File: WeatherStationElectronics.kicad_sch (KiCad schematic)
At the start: 4 parts, among them U1 ESP32-C3-DevKitM-1, U3 DHT11, U4 BMP280

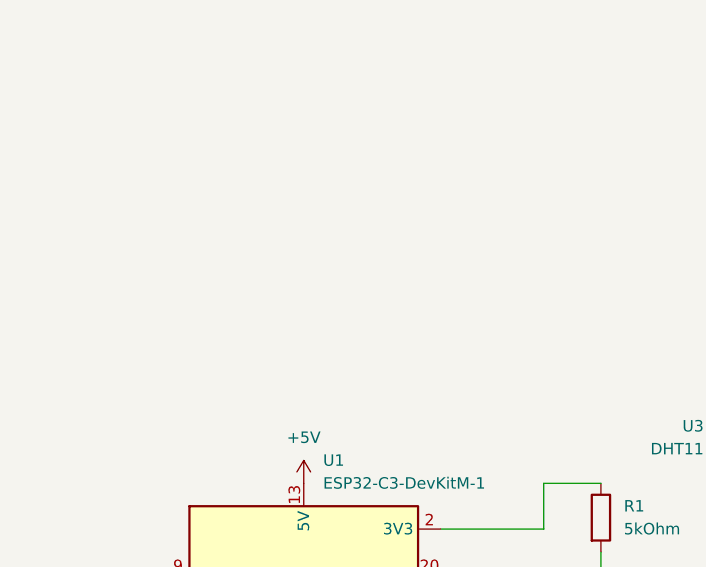
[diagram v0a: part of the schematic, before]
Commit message: first PCB
todo: add a power switch
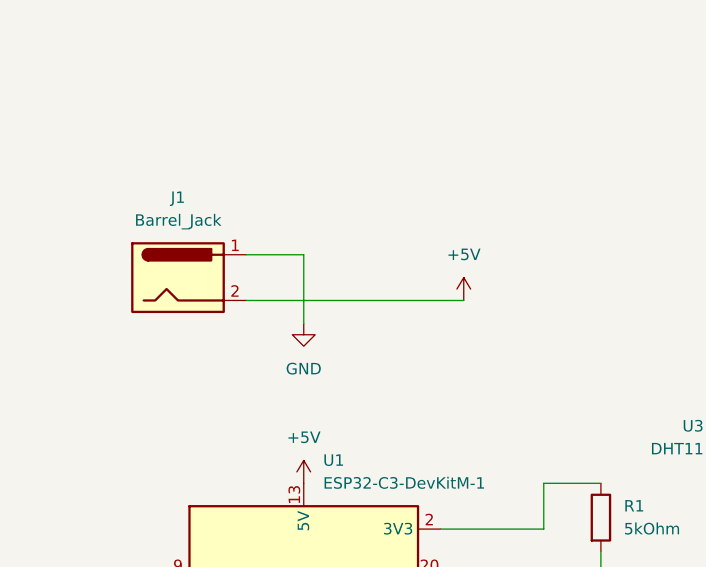
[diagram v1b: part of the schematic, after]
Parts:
- added J1: Barrel_Jack, Connector_BarrelJack:BarrelJack_CUI_PJ-063AH_Horizontal, symbol Connector:Barrel_Jack
- R1: footprint (none) -> Resistor_THT:R_Axial_DIN0411_L9.9mm_D3.6mm_P7.62mm_Vertical
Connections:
- net +5V: now also J1.2
- net GND: now also J1.1
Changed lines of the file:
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@@
+	(wire
+		(pts
+			(xy 68.58 41.91) (xy 68.58 34.29)
+		)
+		(stroke
+			(width 0)
+			(type default)
+		)
+	)
 	(wire
 		(pts
@@
 	(wire
 		(pts
+			(xy 62.23 39.37) (xy 86.36 39.37)
+		)
+		(stroke
+			(width 0)
+			(type default)
+		)
+	)
+	(wire
+		(pts
 			(xy 127 54.61) (xy 127 69.85)
+		)
+		(stroke
+			(width 0)
+			(type default)
+		)
+	)
+	(wire
+		(pts
+			(xy 68.58 34.29) (xy 62.23 34.29)
 		)
 		(stroke
@@
 	)
 	(symbol
+		(lib_id "power:GND")
+		(at 68.58 41.91 0)
+		(unit 1)
+		(exclude_from_sim no)
+		(in_bom yes)
+		(on_board yes)
+		(dnp no)
+		(fields_autoplaced yes)
+		(property "Reference" "#PWR03"
+			(at 68.58 48.26 0)
+			(effects
+				(font
+					(size 1.27 1.27)
+				)
+				(hide yes)
+			)
+		)
+		(property "Value" "GND"
+			(at 68.58 46.99 0)
+			(effects
+				(font
+					(size 1.27 1.27)
+				)
+			)
+		)
+		(property "Footprint" ""
+			(at 68.58 41.91 0)
+			(effects
+				(font
+					(size 1.27 1.27)
+				)
+				(hide yes)
+			)
+		)
+		(property "Datasheet" ""
+			(at 68.58 41.91 0)
+			(effects
+				(font
+					(size 1.27 1.27)
+				)
+				(hide yes)
+			)
+		)
+		(property "Description" "Power symbol creates a global label with name \"GND\" , ground"
+			(at 68.58 41.91 0)
+			(effects
+				(font
+					(size 1.27 1.27)
+				)
+				(hide yes)
+			)
+		)
+		(pin "1"
+		)
+		(instances
+			(project ""
+				(path "/efe9557b-147a-46e1-836e-45cae14ec1c3"
+					(reference "#PWR03")
+					(unit 1)
+				)
+			)
+		)
+	)
+	(symbol
 		(lib_id "power:+5V")
 		(at 68.58 59.69 0)
@@
 	)
 	(symbol
+		(lib_id "Connector:Barrel_Jack")
+		(at 54.61 36.83 0)
+		(unit 1)
+		(exclude_from_sim no)
+		(in_bom yes)
+		(on_board yes)
+		(dnp no)
+		(fields_autoplaced yes)
+		(property "Reference" "J1"
+			(at 54.61 27.94 0)
+			(effects
+				(font
+					(size 1.27 1.27)
+				)
+			)
+		)
+		(property "Value" "Barrel_Jack"
+			(at 54.61 30.48 0)
+			(effects
+				(font
+					(size 1.27 1.27)
+				)
+			)
+		)
+		(property "Footprint" "Connector_BarrelJack:BarrelJack_CUI_PJ-063AH_Horizontal"
+			(at 55.88 37.846 0)
+			(effects
+				(font
+					(size 1.27 1.27)
+				)
+				(hide yes)
+			)
+		)
+		(property "Datasheet" "~"
+			(at 55.88 37.846 0)
+			(effects
+				(font
+					(size 1.27 1.27)
+				)
+				(hide yes)
+			)
+		)
+		(property "Description" "DC Barrel Jack"
+			(at 54.61 36.83 0)
+			(effects
+				(font
+					(size 1.27 1.27)
+				)
+				(hide yes)
+			)
+		)
+		(pin "1"
+		)
+		(pin "2"
+		)
+		(instances
+			(project ""
+				(path "/efe9557b-147a-46e1-836e-45cae14ec1c3"
+					(reference "J1")
+					(unit 1)
+				)
+			)
+		)
+	)
+	(symbol
 		(lib_id "Sensor:DHT11")
 		(at 119.38 54.61 0)
@@
 	)
 	(symbol
+		(lib_id "power:+5V")
+		(at 86.36 39.37 0)
+		(unit 1)
+		(exclude_from_sim no)
+		(in_bom yes)
+		(on_board yes)
+		(dnp no)
+		(fields_autoplaced yes)
+		(property "Reference" "#PWR05"
+			(at 86.36 43.18 0)
+			(effects
+				(font
+					(size 1.27 1.27)
+				)
+				(hide yes)
+			)
+		)
+		(property "Value" "+5V"
+			(at 86.36 34.29 0)
+			(effects
+				(font
+					(size 1.27 1.27)
+				)
+			)
+		)
+		(property "Footprint" ""
+			(at 86.36 39.37 0)
+			(effects
+				(font
+					(size 1.27 1.27)
+				)
+				(hide yes)
+			)
+		)
+		(property "Datasheet" ""
+			(at 86.36 39.37 0)
+			(effects
+				(font
+					(size 1.27 1.27)
+				)
+				(hide yes)
+			)
+		)
+		(property "Description" "Power symbol creates a global label with name \"+5V\""
+			(at 86.36 39.37 0)
+			(effects
+				(font
+					(size 1.27 1.27)
+				)
+				(hide yes)
+			)
+		)
+		(pin "1"
+		)
+		(instances
+			(project ""
+				(path "/efe9557b-147a-46e1-836e-45cae14ec1c3"
+					(reference "#PWR05")
+					(unit 1)
+				)
+			)
+		)
+	)
+	(symbol
 		(lib_id "power:+3.3V")
 		(at 128.27 86.36 0)
@@
 			)
 		)
-		(property "Footprint" ""
+		(property "Footprint" "Resistor_THT:R_Axial_DIN0411_L9.9mm_D3.6mm_P7.62mm_Vertical"
 			(at 99.822 63.5 90)
 			(effects

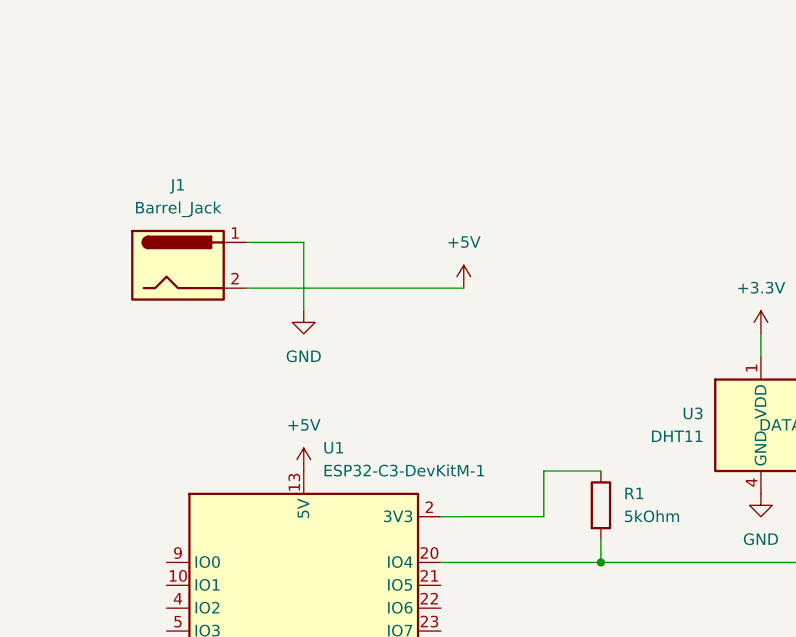
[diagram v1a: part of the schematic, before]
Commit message: update PCB and add a power switch
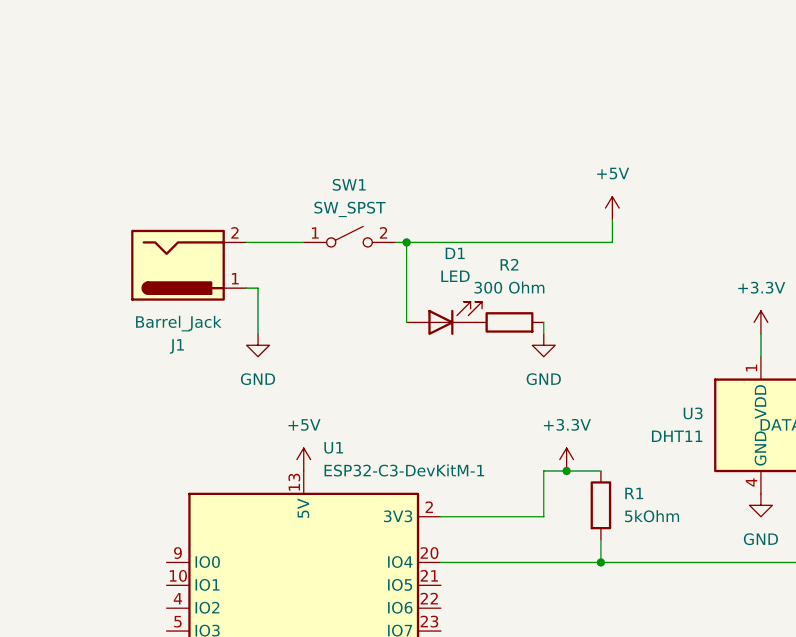
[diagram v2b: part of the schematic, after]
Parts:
- added D1: LED, LED_THT:LED_D5.0mm_Clear, symbol Device:LED
- added R2: 300 Ohm, Resistor_THT:R_Axial_DIN0516_L15.5mm_D5.0mm_P20.32mm_Horizontal, symbol Device:R
- added SW1: SW_SPST, Button_Switch_SMD:SW_MEC_5GSH9, symbol Switch:SW_SPST
- R1: footprint Resistor_THT:R_Axial_DIN0411_L9.9mm_D3.6mm_P7.62mm_Vertical -> Resistor_THT:R_Axial_DIN0411_L9.9mm_D3.6mm_P12.70mm_Horizontal
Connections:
- net +3.3V: now also R1.1, U1.2 (3V3), U1.3 (3V3)
- net +5V: now also D1.2 (A), SW1.2 (B); no longer J1.2
- net GND: now also R2.2
- new net: D1.1 (K), R2.1
- new net: J1.2, SW1.1 (A)
